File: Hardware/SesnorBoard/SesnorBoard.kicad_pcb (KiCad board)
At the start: 2 copper layers, 25 parts, among them U2 CCS811, U3 NC7SVU04P5X, U4 LM324

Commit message: Eerste pcb layouts ensorboard
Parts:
- removed JP1: HEADER POWER & INTERFACE, Connector_PinHeader_1.27mm:PinHeader_1x06_P1.27mm_Horizontal
- removed JP2: HEADER-CONTROL, Connector_PinHeader_1.27mm:PinHeader_1x06_P1.27mm_Horizontal
- removed R22: 1K, Resistor_SMD:R_0805_2012Metric
- removed R23, R24: 10K, Resistor_SMD:R_0805_2012Metric
- removed R25: 100K, Resistor_SMD:R_0805_2012Metric
- removed R26: 100, Resistor_SMD:R_0805_2012Metric
- removed U4: LM324, Package_SO:MSOP-12-1EP_3x4mm_P0.65mm_EP1.65x2.85mm
- added C11: 4.7µF, Capacitor_SMD:C_1206_3216Metric, F.Cu at (68.6, -317.4)
- added J1: Mainboard connection, Connector_PinHeader_1.00mm:PinHeader_1x08_P1.00mm_Vertical, F.Cu at (68.6, -307.1)
- added J2: microphoon connection, Connector_PinHeader_1.00mm:PinHeader_1x03_P1.00mm_Vertical, F.Cu at (63.2, -303.5)
- added R16: 10K, Resistor_SMD:R_1206_3216Metric, B.Cu at (64.1, -307.3)
- added R3: 2k2, Resistor_SMD:R_1206_3216Metric, B.Cu at (64.1, -315.0)
- added R4: 2k2, Resistor_SMD:R_1206_3216Metric, B.Cu at (64.1, -312.4)
- added TH1: 100K, Resistor_SMD:R_1206_3216Metric, F.Cu at (62.9, -319.4)
- added U1: AMG8833, AMG8833_REV-B:AMG8833, F.Cu at (79.4, -310.5)
- C1, C2, C3, C6: footprint Capacitor_SMD:C_0805_2012Metric -> Capacitor_SMD:C_1206_3216Metric; moved to B.Cu
- C21: value 10uF -> 0.1uF; footprint Capacitor_SMD:C_0805_2012Metric -> Capacitor_SMD:C_1206_3216Metric
- D1: value PMEG4050EP -> RB081LAM-20
- R1, R11, R13, R14, R15, R2, R5: footprint Resistor_SMD:R_0805_2012Metric -> Resistor_SMD:R_1206_3216Metric; moved to B.Cu
- R12: value 10K -> 100k; footprint Resistor_SMD:R_0805_2012Metric -> Resistor_SMD:R_1206_3216Metric; moved to B.Cu
- R21: value 2.2K -> 100k; footprint Resistor_SMD:R_0805_2012Metric -> Resistor_SMD:R_1206_3216Metric
- U3: moved to B.Cu
- moved R13 32.1 mm to (80.0, -317.5), turned to 270 degrees
- moved R12 27.8 mm to (68.6, -317.4), turned to 270 degrees
- moved R21 27.8 mm to (62.2, -313.1)
- moved U2 26.1 mm to (71.9, -317.5), turned to 270 degrees
- moved U3 25.4 mm to (71.8, -311.1), turned to 180 degrees
- moved R1 20.8 mm to (64.1, -309.9), turned to 180 degrees
- moved R14 20.7 mm to (76.2, -317.5), turned to 90 degrees
- moved C21 20.5 mm to (62.2, -310.5)
- moved R15 17.2 mm to (71.1, -306.7), turned to 270 degrees
- moved R11 15.5 mm to (82.5, -317.5), turned to 90 degrees
- moved R2 14.5 mm to (76.8, -311.1)
- moved C3 12.4 mm to (76.8, -313.7), turned to 180 degrees
- moved R5 11.2 mm to (79.4, -304.8), turned to 270 degrees
- moved C1 9.76 mm to (76.8, -304.8), turned to 90 degrees
- moved D1 8.72 mm to (62.2, -307.3)
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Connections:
- C21 pad 1: Net-(C21-Pad1) -> /DETECTOR_OUT
- C21 pad 2: Net-(C21-Pad2) -> GND
- D1 pad 1: /DETECTOR-OUT -> /DETECTOR_OUT
- R11 pad 1: +3V3 -> 3.3V
- R12 pad 1: /INT_CSS811 -> Net-(R12-Pad1)
- R12 pad 2: +3V3 -> 3.3V
- R13 pad 2: +3V3 -> 3.3V
- R21 pad 1: Net-(C21-Pad2) -> /DETECTOR_OUT
- R21 pad 2: 3.3V -> GND
- U2 pad 6: +3V3 -> 3.3V
- U2 pad 8: Net-(TH1-Pad1) (its old number) -> Net-(R12-Pad1)
- U3 pad 4: /INT_CSS811 -> /nINT_CCS811
- U3 pad 5: +3V3 -> 3.3V
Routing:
- net GND: track 0.00 -> 72.2 mm, vias 0 -> 2
- net 3.3V: track 0.00 -> 67.2 mm, vias 0 -> 2
- net /DETECTOR_OUT: track 0.00 -> 22.4 mm
- net /SCL: track 0.00 -> 21.7 mm
- net /SDA: track 0.00 -> 18.0 mm
- net Net-(R12-Pad1): track 0.00 -> 14.9 mm, vias 0 -> 2
- net /nINT: track 0.00 -> 14.8 mm, vias 0 -> 1
- net Net-(R11-Pad2): track 0.00 -> 13.0 mm, vias 0 -> 1
- net /nWAKE: track 0.00 -> 12.0 mm, vias 0 -> 1
- net /INT_AMG8833: track 0.00 -> 11.8 mm
- net Net-(TH1-Pad1): track 0.00 -> 9.90 mm
- net Net-(R13-Pad1): track 0.00 -> 8.24 mm, vias 0 -> 1
- net Net-(C3-Pad1): track 0.00 -> 7.48 mm, vias 0 -> 1
- net /nINT_CCS811: track 0.00 -> 6.84 mm
- net Net-(C2-Pad2): track 0.00 -> 5.22 mm
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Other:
- board outline added: 29.2 x 21 mm

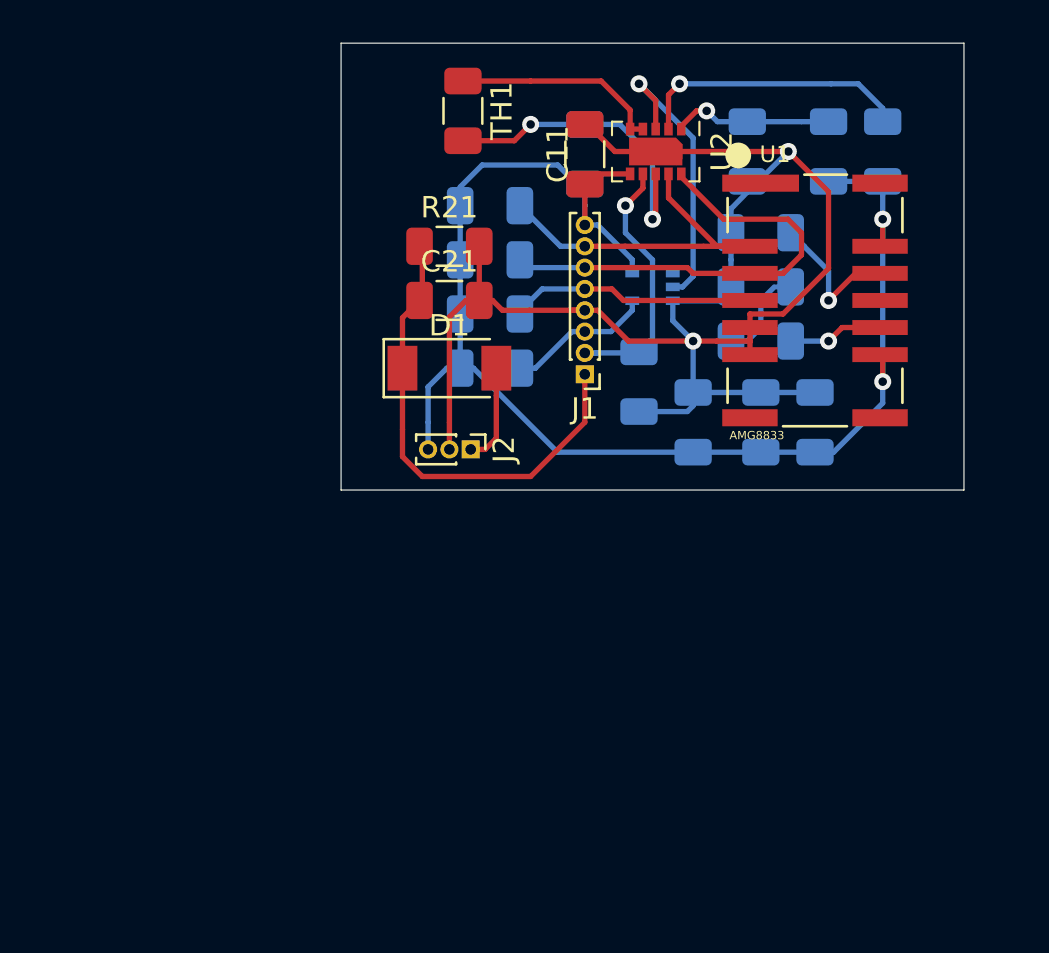
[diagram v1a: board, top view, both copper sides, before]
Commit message: SEnsorboard PCB adapted to normal siezd pinheader
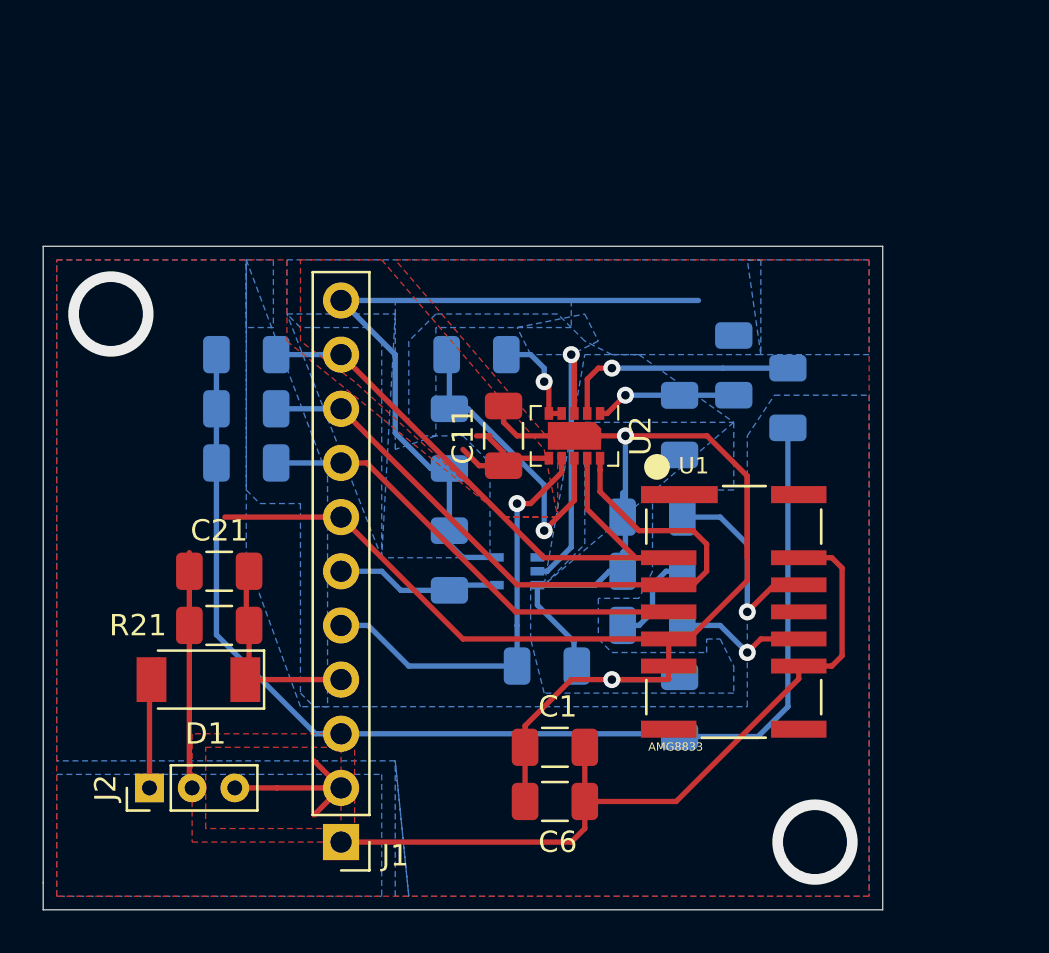
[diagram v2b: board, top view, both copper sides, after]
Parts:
- C1, C6: moved to F.Cu
- J1: footprint Connector_PinHeader_1.00mm:PinHeader_1x08_P1.00mm_Vertical -> Connector_PinHeader_2.54mm:PinHeader_1x11_P2.54mm_Vertical
- J2: footprint Connector_PinHeader_1.00mm:PinHeader_1x03_P1.00mm_Vertical -> Connector_PinHeader_2.00mm:PinHeader_1x03_P2.00mm_Vertical
- TH1: moved to B.Cu
- moved J1 24.7 mm to (57.1, -285.1)
- moved J2 21.9 mm to (48.2, -287.7), turned to 90 degrees
- moved R21 20.8 mm to (51.4, -295.3), turned to 180 degrees
- moved C6 18.9 mm to (67.2, -287.0), turned to 180 degrees
- moved D1 18.8 mm to (50.5, -292.7), turned to 180 degrees
- moved C1 18.0 mm to (67.2, -289.6), turned to 180 degrees
- moved C21 16.7 mm to (51.4, -297.8), turned to 180 degrees
- moved U1 15.1 mm to (75.6, -295.9)
- moved R5 14.8 mm to (73.0, -291.5)
- moved R12 14.8 mm to (62.2, -304.0)
- moved U3 14.8 mm to (65.4, -297.8)
- moved C2 14.3 mm to (71.8, -295.3)
- moved C3 14.3 mm to (71.8, -300.4)
- moved R2 14.3 mm to (71.8, -297.8)
- moved R15 14.0 mm to (66.8, -293.4), turned to 0 degrees
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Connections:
- C1 pad 1: 3.3V -> /AMG8833_3V3
- C11 pad 1: 3.3V -> /CCS811_3V3
- C6 pad 1: 3.3V -> /AMG8833_3V3
- J1 pad 1: /DETECTOR_OUT -> /AMG8833_3V3
- J1 pad 2: /nWAKE -> /AUDIO_3V3
- J1 pad 3: /nINT_CCS811 -> 3.3V
- J1 pad 4: GND -> /DETECTOR_OUT
- J1 pad 5: /INT_AMG8833 -> /nWAKE
- J1 pad 6: /SCL -> /nINT_CCS811
- J1 pad 7: /SDA -> GND
- J1 pad 8: 3.3V -> /INT_AMG8833
- J2 pad 3: 3.3V -> /AUDIO_3V3
- R12 pad 2: 3.3V -> /CCS811_3V3
- R13 pad 2: 3.3V -> /CCS811_3V3
- R16 pad 2: 3.3V -> /CCS811_3V3
- U1 pad 13: 3.3V -> /AMG8833_3V3
- U1 pad 9: 3.3V -> /AMG8833_3V3
- U2 pad 6: 3.3V -> /CCS811_3V3
- U3 pad 5: 3.3V -> /CCS811_3V3
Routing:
- net /CCS811_3V3: track 0.00 -> 40.4 mm
- net /AMG8833_3V3: track 0.00 -> 38.1 mm
- net GND: track 72.2 -> 95.9 mm, vias 2 -> 4
- net /DETECTOR_OUT: track 22.4 -> 9.64 mm
- net /SDA: track 18.0 -> 30.7 mm
- net /SCL: track 21.7 -> 32.9 mm
- net 3.3V: track 67.2 -> 56.9 mm, vias 2 -> 0
- net /INT_AMG8833: track 11.8 -> 21.6 mm
- net /AUDIO_3V3: track 0.00 -> 8.58 mm
- net /nWAKE: track 12.0 -> 20.3 mm
- net Net-(TH1-Pad1): track 9.90 -> 4.92 mm, vias 0 -> 1
- net Net-(C3-Pad1): track 7.48 -> 9.69 mm
- net Net-(C2-Pad1): track 4.45 -> 6.43 mm
- net Net-(R11-Pad2): track 13.0 -> 11.2 mm
- net /AUDIO_OUT: track 4.70 -> 6.39 mm
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- added copper zone on B.Cu, net /AUDIO_3V3
- added copper zone on F.Cu, net /AUDIO_3V3
- added copper zone on B.Cu, net /CCS811_3V3
- added copper zone on F.Cu, net /CCS811_3V3
- added copper zone on B.Cu, net 3.3V
- added copper zone on B.Cu, net GND
- added copper zone on F.Cu, net GND
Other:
- board size 29.2 x 21 mm -> 39.4 x 31.1 mm
- board text added: "All holes are plated holes with finished hole sizes"

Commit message: insert pinnames on J1
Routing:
- net GND: track 95.9 -> 100.4 mm
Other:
- board text added: "3.3V"
- board text added: "AMG8833_3V3"
- board text added: "AUDIO 3V3"
- board text added: "CCS811_3V3"
- board text added: "DETECTOR_OUT"
- board text added: "GND"
- board text added: "INT_AMG8833"
- board text added: "SCL"
- board text added: "SDA"
- board text added: "nINT_CCS811"
- board text added: "nWAKE"
